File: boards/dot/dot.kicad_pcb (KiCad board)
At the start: 2 copper layers, 45.7 x 45.7 mm, 6 parts, among them J21 CONN_01X02, J22 CONN_01X02, J28 CONN_01X02, U92 APA102C_x2, U95 APA102C_x3, U99 APA102C_x2

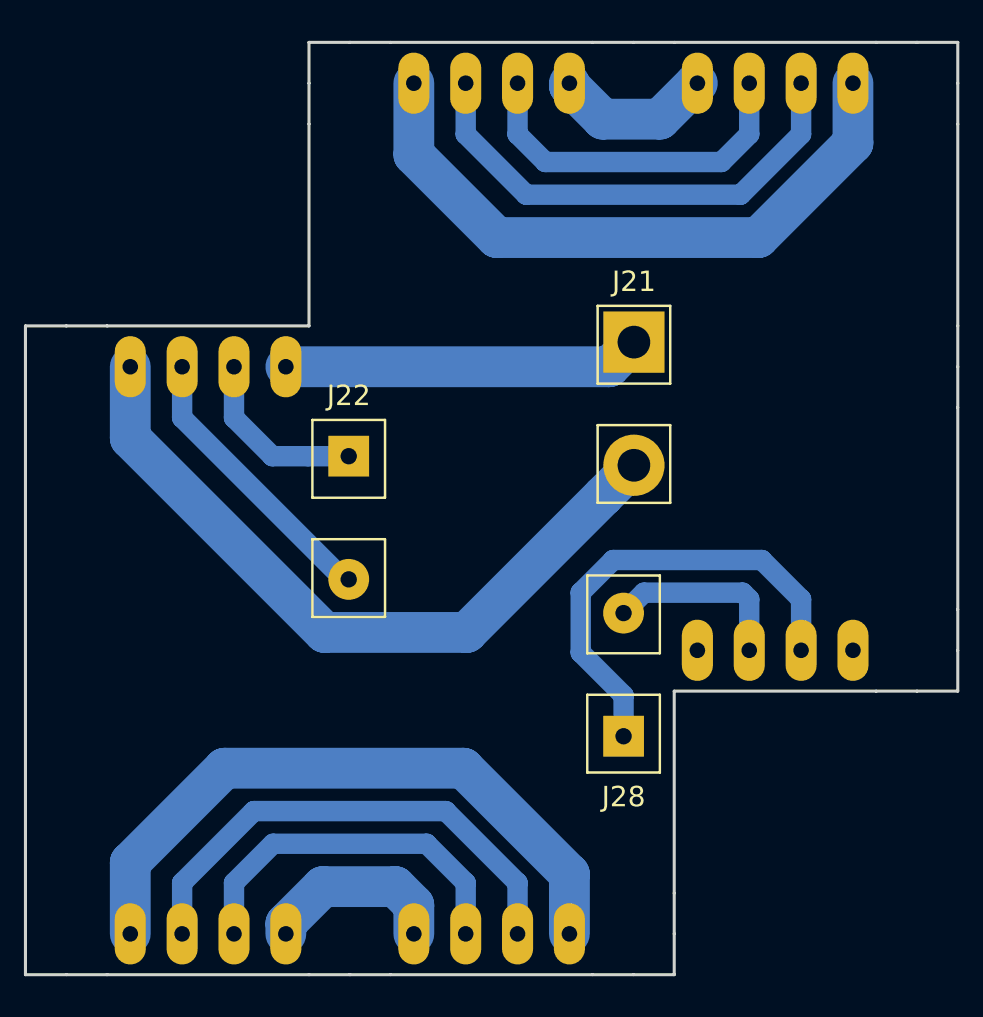
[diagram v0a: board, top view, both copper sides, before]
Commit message: Generate gerbers for all letters. Use a single drill size.
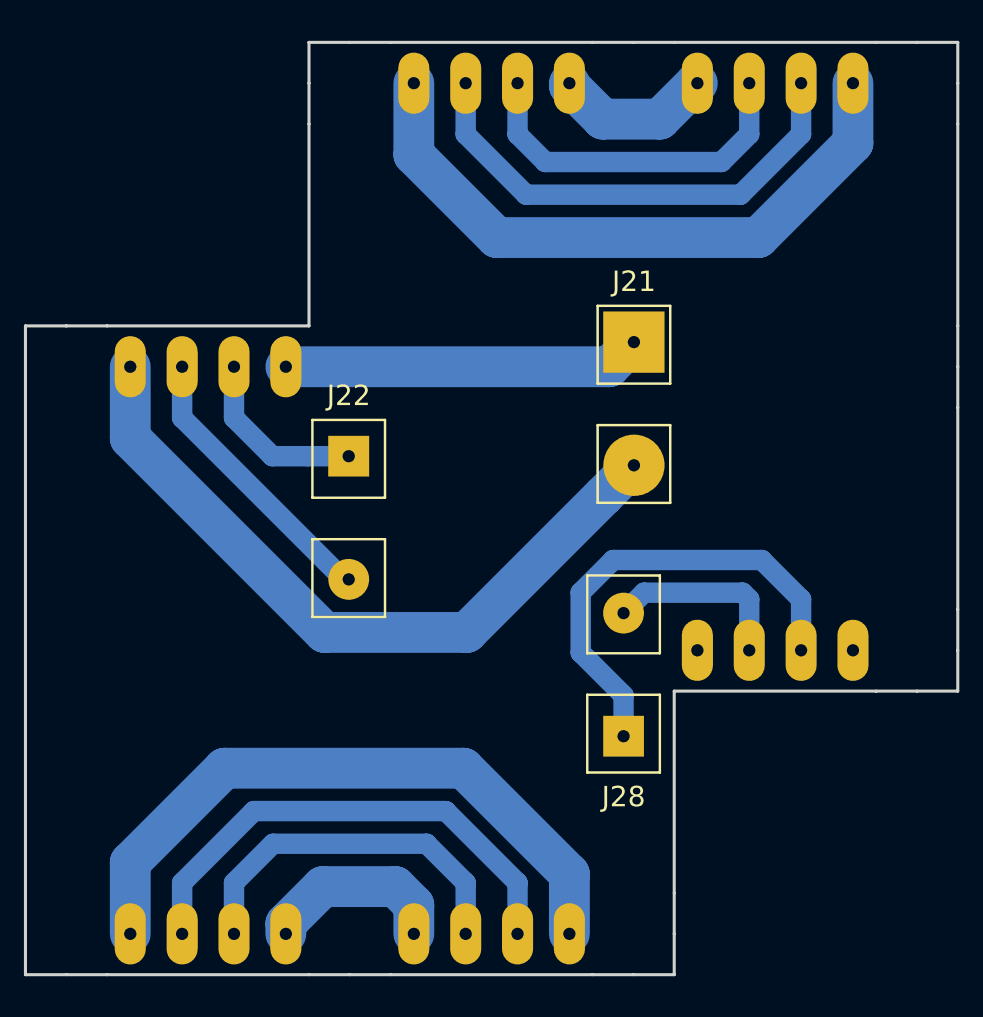
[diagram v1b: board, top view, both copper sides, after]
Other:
- net class Default: via_drill 0.4 -> 0.6
- net class Signal: via_drill 0.4 -> 0.6
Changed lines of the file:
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@@
   (general
     (links 14)
-    (no_connects 2)
-    (area 403.758299 369.036099 546.797201 414.852801)
+    (no_connects 0)
+    (area 33.874599 31.9531 79.691201 77.8198)
     (thickness 1.6)
     (drawings 44)
@@
     (edge_width 0.15)
     (via_size 0.6)
-    (via_drill 0.4)
+    (via_drill 0.6)
     (via_min_size 0.4)
     (via_min_drill 0.3)
@@
     (mod_text_width 0.15)
     (pad_size 1.524 1.524)
-    (pad_drill 0.762)
+    (pad_drill 0.6)
     (pad_to_mask_clearance 0.2)
     (aux_axis_origin 0 0)
     (visible_elements FFFFFFFF)
     (pcbplotparams
-      (layerselection 0x01000_80000001)
+      (layerselection 0x01000_80000000)
       (usegerberextensions false)
       (excludeedgelayer true)
@@
       (padsonsilk false)
       (subtractmaskfromsilk false)
-      (outputformat 5)
+      (outputformat 1)
       (mirror false)
       (drillshape 0)
@@
     (trace_width 2)
     (via_dia 0.6)
-    (via_drill 0.4)
+    (via_drill 0.6)
     (uvia_dia 0.3)
     (uvia_drill 0.1)
@@
     (trace_width 1)
     (via_dia 0.6)
-    (via_drill 0.4)
+    (via_drill 0.6)
     (uvia_dia 0.3)
     (uvia_drill 0.1)
@@
     (fp_line (start 13.8889 5.08) (end 13.8889 -5.08) (layer B.CrtYd) (width 0.15))
     (fp_line (start -13.8889 5.08) (end 13.8889 5.08) (layer B.CrtYd) (width 0.15))
-    (pad 1 thru_hole oval (at -13.8889 -3.81 270) (size 3 1.524) (drill 0.762) (layers *.Cu *.Mask)
+    (pad 1 thru_hole oval (at -13.8889 -3.81 270) (size 3 1.524) (drill 0.6) (layers *.Cu *.Mask)
       (net 2 GND))
-    (pad 2 thru_hole oval (at -13.8889 -1.27 270) (size 3 1.524) (drill 0.762) (layers *.Cu *.Mask)
+    (pad 2 thru_hole oval (at -13.8889 -1.27 270) (size 3 1.524) (drill 0.6) (layers *.Cu *.Mask)
       (net 11 "Net-(J22-Pad1)"))
-    (pad 3 thru_hole oval (at -13.8889 1.27 270) (size 3 1.524) (drill 0.762) (layers *.Cu *.Mask)
+    (pad 3 thru_hole oval (at -13.8889 1.27 270) (size 3 1.524) (drill 0.6) (layers *.Cu *.Mask)
       (net 12 "Net-(J22-Pad2)"))
-    (pad 4 thru_hole oval (at -13.8889 3.81 270) (size 3 1.524) (drill 0.762) (layers *.Cu *.Mask)
+    (pad 4 thru_hole oval (at -13.8889 3.81 270) (size 3 1.524) (drill 0.6) (layers *.Cu *.Mask)
       (net 1 +5V))
-    (pad 5 thru_hole oval (at 13.8889 -3.81 270) (size 3 1.524) (drill 0.762) (layers *.Cu *.Mask)
+    (pad 5 thru_hole oval (at 13.8889 -3.81 270) (size 3 1.524) (drill 0.6) (layers *.Cu *.Mask)
       (net 3 "Net-(U92-Pad5)"))
-    (pad 6 thru_hole oval (at 13.8889 -1.27 270) (size 3 1.524) (drill 0.762) (layers *.Cu *.Mask)
+    (pad 6 thru_hole oval (at 13.8889 -1.27 270) (size 3 1.524) (drill 0.6) (layers *.Cu *.Mask)
       (net 4 "Net-(U92-Pad6)"))
-    (pad 7 thru_hole oval (at 13.8889 1.27 270) (size 3 1.524) (drill 0.762) (layers *.Cu *.Mask)
+    (pad 7 thru_hole oval (at 13.8889 1.27 270) (size 3 1.524) (drill 0.6) (layers *.Cu *.Mask)
       (net 5 "Net-(U92-Pad7)"))
-    (pad 8 thru_hole oval (at 13.8889 3.81 270) (size 3 1.524) (drill 0.762) (layers *.Cu *.Mask)
+    (pad 8 thru_hole oval (at 13.8889 3.81 270) (size 3 1.524) (drill 0.6) (layers *.Cu *.Mask)
       (net 6 "Net-(U92-Pad8)"))
   )
@@
     (fp_line (start 20.8333 5.08) (end 20.8333 -5.08) (layer B.CrtYd) (width 0.15))
     (fp_line (start -20.8333 5.08) (end 20.8333 5.08) (layer B.CrtYd) (width 0.15))
-    (pad 1 thru_hole oval (at -20.8333 -3.81 90) (size 3 1.524) (drill 0.762) (layers *.Cu *.Mask)
+    (pad 1 thru_hole oval (at -20.8333 -3.81 90) (size 3 1.524) (drill 0.6) (layers *.Cu *.Mask)
       (net 3 "Net-(U92-Pad5)"))
-    (pad 2 thru_hole oval (at -20.8333 -1.27 90) (size 3 1.524) (drill 0.762) (layers *.Cu *.Mask)
+    (pad 2 thru_hole oval (at -20.8333 -1.27 90) (size 3 1.524) (drill 0.6) (layers *.Cu *.Mask)
       (net 4 "Net-(U92-Pad6)"))
-    (pad 3 thru_hole oval (at -20.8333 1.27 90) (size 3 1.524) (drill 0.762) (layers *.Cu *.Mask)
+    (pad 3 thru_hole oval (at -20.8333 1.27 90) (size 3 1.524) (drill 0.6) (layers *.Cu *.Mask)
       (net 5 "Net-(U92-Pad7)"))
-    (pad 4 thru_hole oval (at -20.8333 3.81 90) (size 3 1.524) (drill 0.762) (layers *.Cu *.Mask)
+    (pad 4 thru_hole oval (at -20.8333 3.81 90) (size 3 1.524) (drill 0.6) (layers *.Cu *.Mask)
       (net 6 "Net-(U92-Pad8)"))
-    (pad 5 thru_hole oval (at 20.8333 -3.81 90) (size 3 1.524) (drill 0.762) (layers *.Cu *.Mask)
+    (pad 5 thru_hole oval (at 20.8333 -3.81 90) (size 3 1.524) (drill 0.6) (layers *.Cu *.Mask)
       (net 7 "Net-(U95-Pad5)"))
-    (pad 6 thru_hole oval (at 20.8333 -1.27 90) (size 3 1.524) (drill 0.762) (layers *.Cu *.Mask)
+    (pad 6 thru_hole oval (at 20.8333 -1.27 90) (size 3 1.524) (drill 0.6) (layers *.Cu *.Mask)
       (net 8 "Net-(U95-Pad6)"))
-    (pad 7 thru_hole oval (at 20.8333 1.27 90) (size 3 1.524) (drill 0.762) (layers *.Cu *.Mask)
+    (pad 7 thru_hole oval (at 20.8333 1.27 90) (size 3 1.524) (drill 0.6) (layers *.Cu *.Mask)
       (net 9 "Net-(U95-Pad7)"))
-    (pad 8 thru_hole oval (at 20.8333 3.81 90) (size 3 1.524) (drill 0.762) (layers *.Cu *.Mask)
+    (pad 8 thru_hole oval (at 20.8333 3.81 90) (size 3 1.524) (drill 0.6) (layers *.Cu *.Mask)
       (net 10 "Net-(U95-Pad8)"))
   )
@@
     (fp_line (start 13.8889 5.08) (end 13.8889 -5.08) (layer B.CrtYd) (width 0.15))
     (fp_line (start -13.8889 5.08) (end 13.8889 5.08) (layer B.CrtYd) (width 0.15))
-    (pad 1 thru_hole oval (at -13.8889 -3.81 270) (size 3 1.524) (drill 0.762) (layers *.Cu *.Mask)
+    (pad 1 thru_hole oval (at -13.8889 -3.81 270) (size 3 1.524) (drill 0.6) (layers *.Cu *.Mask)
       (net 7 "Net-(U95-Pad5)"))
-    (pad 2 thru_hole oval (at -13.8889 -1.27 270) (size 3 1.524) (drill 0.762) (layers *.Cu *.Mask)
+    (pad 2 thru_hole oval (at -13.8889 -1.27 270) (size 3 1.524) (drill 0.6) (layers *.Cu *.Mask)
       (net 8 "Net-(U95-Pad6)"))
-    (pad 3 thru_hole oval (at -13.8889 1.27 270) (size 3 1.524) (drill 0.762) (layers *.Cu *.Mask)
+    (pad 3 thru_hole oval (at -13.8889 1.27 270) (size 3 1.524) (drill 0.6) (layers *.Cu *.Mask)
       (net 9 "Net-(U95-Pad7)"))
-    (pad 4 thru_hole oval (at -13.8889 3.81 270) (size 3 1.524) (drill 0.762) (layers *.Cu *.Mask)
+    (pad 4 thru_hole oval (at -13.8889 3.81 270) (size 3 1.524) (drill 0.6) (layers *.Cu *.Mask)
       (net 10 "Net-(U95-Pad8)"))
-    (pad 5 thru_hole oval (at 13.8889 -3.81 270) (size 3 1.524) (drill 0.762) (layers *.Cu *.Mask))
-    (pad 6 thru_hole oval (at 13.8889 -1.27 270) (size 3 1.524) (drill 0.762) (layers *.Cu *.Mask)
+    (pad 5 thru_hole oval (at 13.8889 -3.81 270) (size 3 1.524) (drill 0.6) (layers *.Cu *.Mask))
+    (pad 6 thru_hole oval (at 13.8889 -1.27 270) (size 3 1.524) (drill 0.6) (layers *.Cu *.Mask)
       (net 13 "Net-(J28-Pad1)"))
-    (pad 7 thru_hole oval (at 13.8889 1.27 270) (size 3 1.524) (drill 0.762) (layers *.Cu *.Mask)
+    (pad 7 thru_hole oval (at 13.8889 1.27 270) (size 3 1.524) (drill 0.6) (layers *.Cu *.Mask)
       (net 14 "Net-(J28-Pad2)"))
-    (pad 8 thru_hole oval (at 13.8889 3.81 270) (size 3 1.524) (drill 0.762) (layers *.Cu *.Mask))
+    (pad 8 thru_hole oval (at 13.8889 3.81 270) (size 3 1.524) (drill 0.6) (layers *.Cu *.Mask))
   )
   (module connector:Sign_Connector (layer F.Cu)
@@
     (fp_line (start 1.778 0) (end 1.778 -3.81) (layer F.SilkS) (width 0.12))
     (fp_line (start -1.778 -3.81) (end 1.778 -3.81) (layer F.SilkS) (width 0.12))
-    (pad 1 thru_hole rect (at 0 -2.032 180) (size 2 2) (drill 0.8) (layers *.Cu *.Mask)
+    (pad 1 thru_hole rect (at 0 -2.032 180) (size 2 2) (drill 0.6) (layers *.Cu *.Mask)
       (net 13 "Net-(J28-Pad1)"))
-    (pad 2 thru_hole oval (at 0 4 180) (size 2 2) (drill 0.8) (layers *.Cu *.Mask)
+    (pad 2 thru_hole oval (at 0 4 180) (size 2 2) (drill 0.6) (layers *.Cu *.Mask)
       (net 14 "Net-(J28-Pad2)"))
     (model ${KISYS3DMOD}/Pin_Headers.3dshapes/Pin_Header_Straight_1x02_Pitch2.54mm.wrl
@@
     (fp_line (start 1.778 0) (end 1.778 -3.81) (layer F.SilkS) (width 0.12))
     (fp_line (start -1.778 -3.81) (end 1.778 -3.81) (layer F.SilkS) (width 0.12))
-    (pad 1 thru_hole rect (at 0 -2.032) (size 2 2) (drill 0.8) (layers *.Cu *.Mask)
+    (pad 1 thru_hole rect (at 0 -2.032) (size 2 2) (drill 0.6) (layers *.Cu *.Mask)
       (net 11 "Net-(J22-Pad1)"))
-    (pad 2 thru_hole oval (at 0 4) (size 2 2) (drill 0.8) (layers *.Cu *.Mask)
+    (pad 2 thru_hole oval (at 0 4) (size 2 2) (drill 0.6) (layers *.Cu *.Mask)
       (net 12 "Net-(J22-Pad2)"))
     (model ${KISYS3DMOD}/Pin_Headers.3dshapes/Pin_Header_Straight_1x02_Pitch2.54mm.wrl
@@
     (fp_line (start 1.778 0) (end 1.778 -3.81) (layer F.SilkS) (width 0.12))
     (fp_line (start -1.778 -3.81) (end 1.778 -3.81) (layer F.SilkS) (width 0.12))
-    (pad 1 thru_hole rect (at 0 -2.032) (size 3 3) (drill 1.6) (layers *.Cu *.Mask)
+    (pad 1 thru_hole rect (at 0 -2.032) (size 3 3) (drill 0.6) (layers *.Cu *.Mask)
       (net 2 GND))
-    (pad 2 thru_hole oval (at 0 4) (size 3 3) (drill 1.6) (layers *.Cu *.Mask)
+    (pad 2 thru_hole oval (at 0 4) (size 3 3) (drill 0.6) (layers *.Cu *.Mask)
       (net 1 +5V))
     (model ${KISYS3DMOD}/Pin_Headers.3dshapes/Pin_Header_Straight_1x02_Pitch2.54mm.wrl

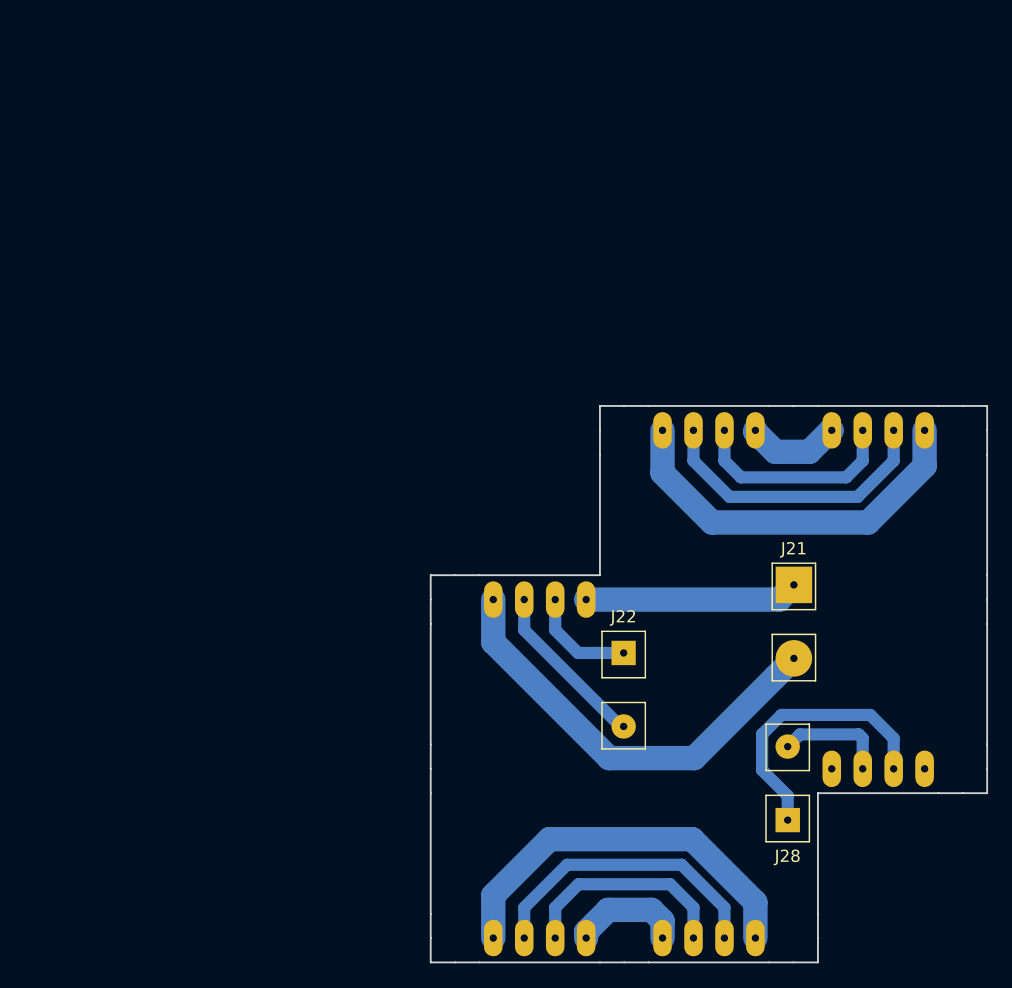
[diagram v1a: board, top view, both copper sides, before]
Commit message: Add flatcam workflow for 'dot'
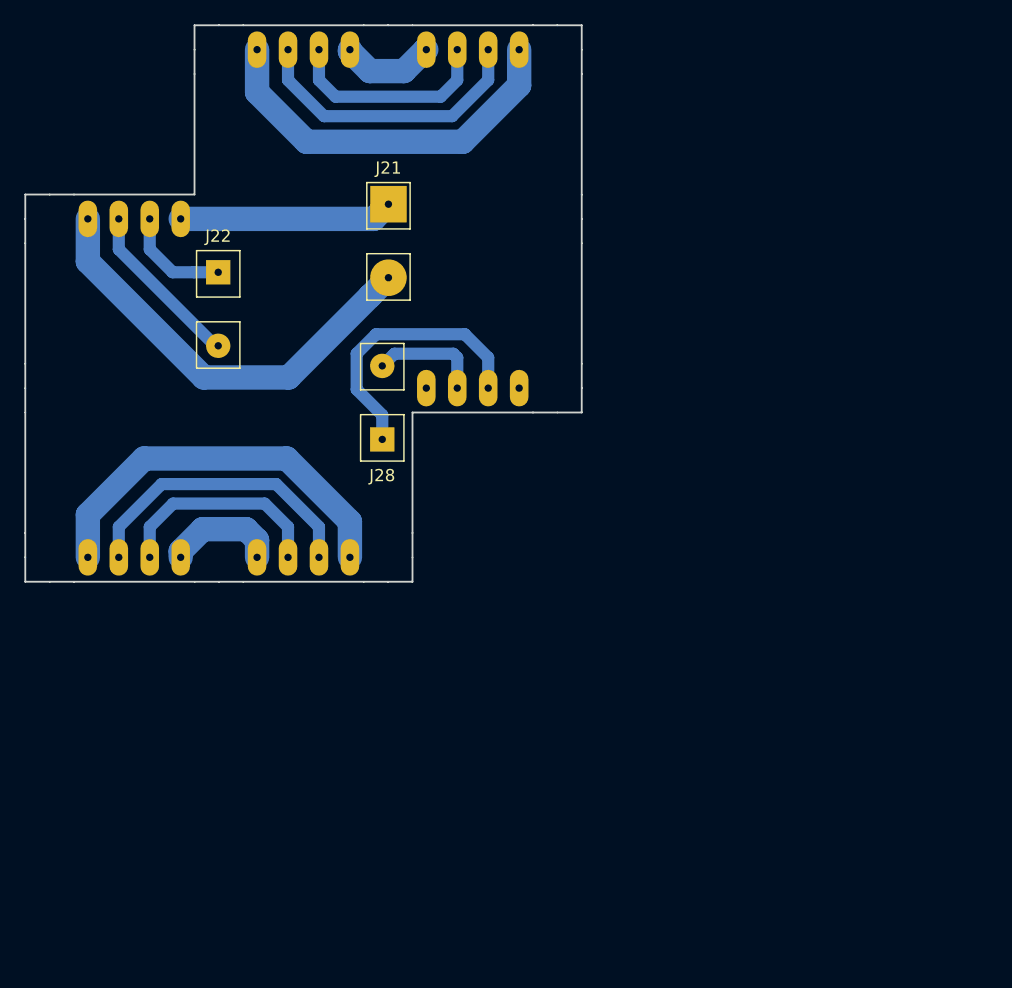
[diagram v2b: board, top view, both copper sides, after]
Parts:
- moved U99 45.6 mm to (37.4, 16.7)
- moved J21 45.6 mm to (30.5, 17.5)
- moved J22 45.6 mm to (16.5, 23.1)
- moved J28 45.6 mm to (30.0, 32.8)
- moved U92 45.6 mm to (9.62, 30.6)
- moved U95 45.6 mm to (23.5, 23.6)
